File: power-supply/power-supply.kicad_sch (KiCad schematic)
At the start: 12 parts, among them J1 Conn_01x04, Q1 Q_PMOS_GSD, Q3 Q_NMOS_GSD, U1 AZ1084-5.0

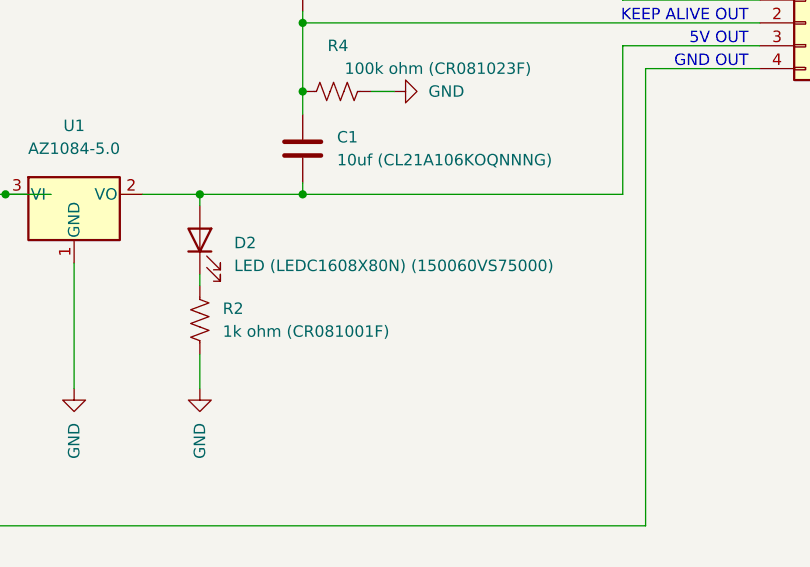
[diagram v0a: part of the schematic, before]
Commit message: Rearranged onto a smaller board
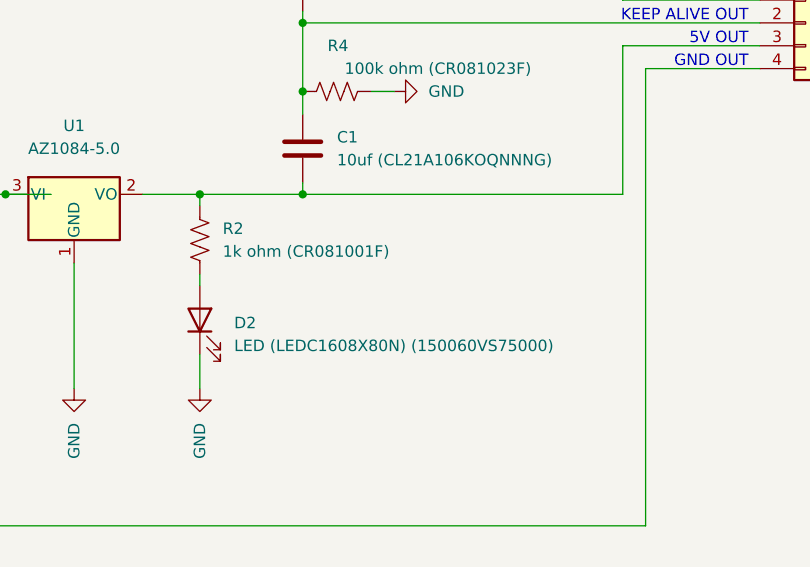
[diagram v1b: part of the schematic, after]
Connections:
- net GND: now also D2.1 (K); no longer R2.1
- net at R2.2: now also C1.2, J1.3 (Pin_3), U1.2 (VO); no longer D2.1 (K)
- new net: D2.2 (A), R2.1
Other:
- moved on the sheet: D2, R2
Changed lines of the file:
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@@
     (pin "2")
   )
-  (symbol (lib_id "Device:LED") (at 111.76 107.95 90) (unit 1)
+  (symbol (lib_id "Device:LED") (at 111.76 116.84 90) (unit 1)
     (in_bom yes) (on_board yes) (fields_autoplaced)
-    (property "Reference" "D2" (id 0) (at 115.57 108.2674 90)
+    (property "Reference" "D2" (id 0) (at 115.57 117.1574 90)
       (effects (font (size 1.27 1.27)) (justify right))
     )
-    (property "Value" "LED (LEDC1608X80N) (150060VS75000)" (id 1) (at 115.57 110.8074 90)
+    (property "Value" "LED (LEDC1608X80N) (150060VS75000)" (id 1) (at 115.57 119.6974 90)
       (effects (font (size 1.27 1.27)) (justify right))
     )
-    (property "Footprint" "LED_SMD:LED_0603_1608Metric" (id 2) (at 111.76 107.95 0)
+    (property "Footprint" "LED_SMD:LED_0603_1608Metric" (id 2) (at 111.76 116.84 0)
       (effects (font (size 1.27 1.27)) hide)
     )
-    (property "Datasheet" "~" (id 3) (at 111.76 107.95 0)
+    (property "Datasheet" "~" (id 3) (at 111.76 116.84 0)
       (effects (font (size 1.27 1.27)) hide)
     )
@@
     (pin "1")
   )
-  (symbol (lib_id "Device:R_US") (at 111.76 116.84 180) (unit 1)
+  (symbol (lib_id "Device:R_US") (at 111.76 107.95 180) (unit 1)
     (in_bom yes) (on_board yes) (fields_autoplaced)
-    (property "Reference" "R2" (id 0) (at 114.3 115.5699 0)
+    (property "Reference" "R2" (id 0) (at 114.3 106.6799 0)
       (effects (font (size 1.27 1.27)) (justify right))
     )
-    (property "Value" "1k ohm (CR081001F)" (id 1) (at 114.3 118.1099 0)
+    (property "Value" "1k ohm (CR081001F)" (id 1) (at 114.3 109.2199 0)
       (effects (font (size 1.27 1.27)) (justify right))
     )
-    (property "Footprint" "Resistor_SMD:R_1206_3216Metric" (id 2) (at 110.744 116.586 90)
+    (property "Footprint" "Resistor_SMD:R_1206_3216Metric" (id 2) (at 110.744 107.696 90)
       (effects (font (size 1.27 1.27)) hide)
     )
-    (property "Datasheet" "~" (id 3) (at 111.76 116.84 0)
+    (property "Datasheet" "~" (id 3) (at 111.76 107.95 0)
       (effects (font (size 1.27 1.27)) hide)
     )
